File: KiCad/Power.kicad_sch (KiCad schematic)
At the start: 0 parts

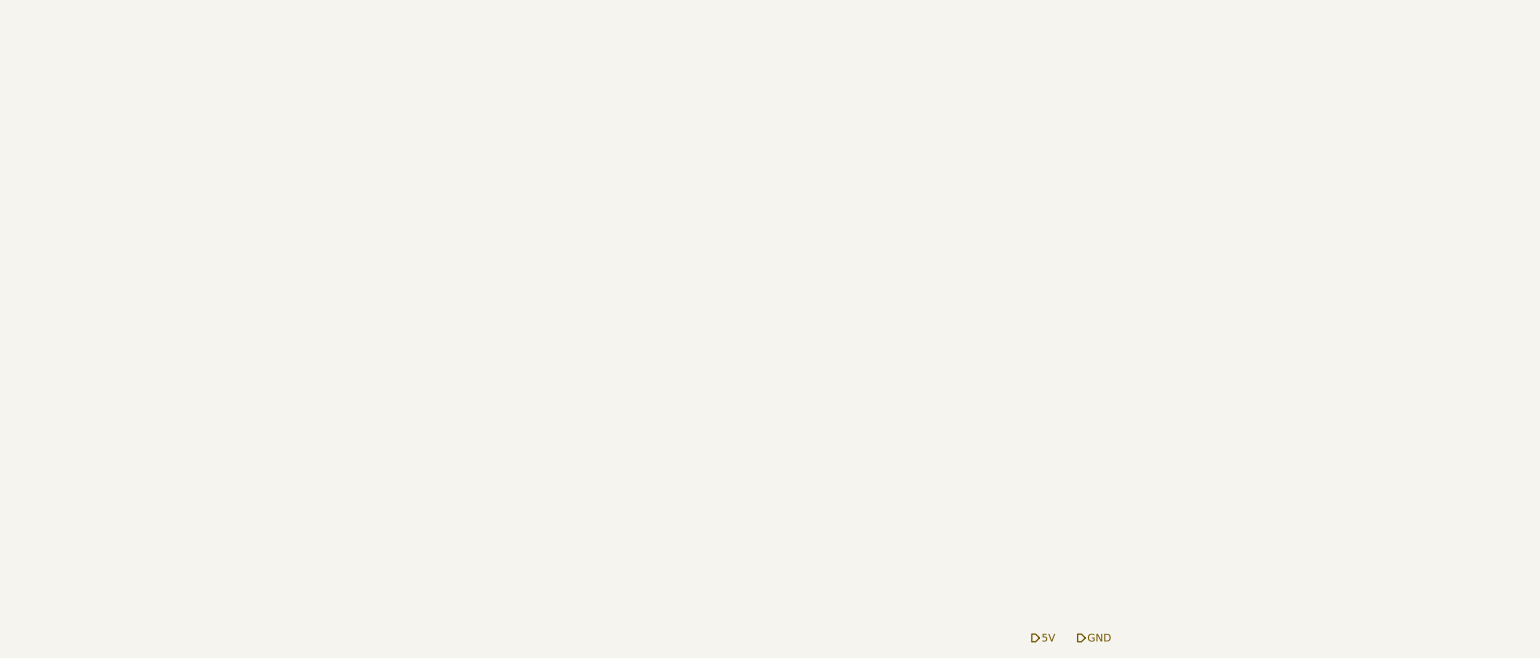
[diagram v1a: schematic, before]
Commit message: kicad power added
added the power section to kicad
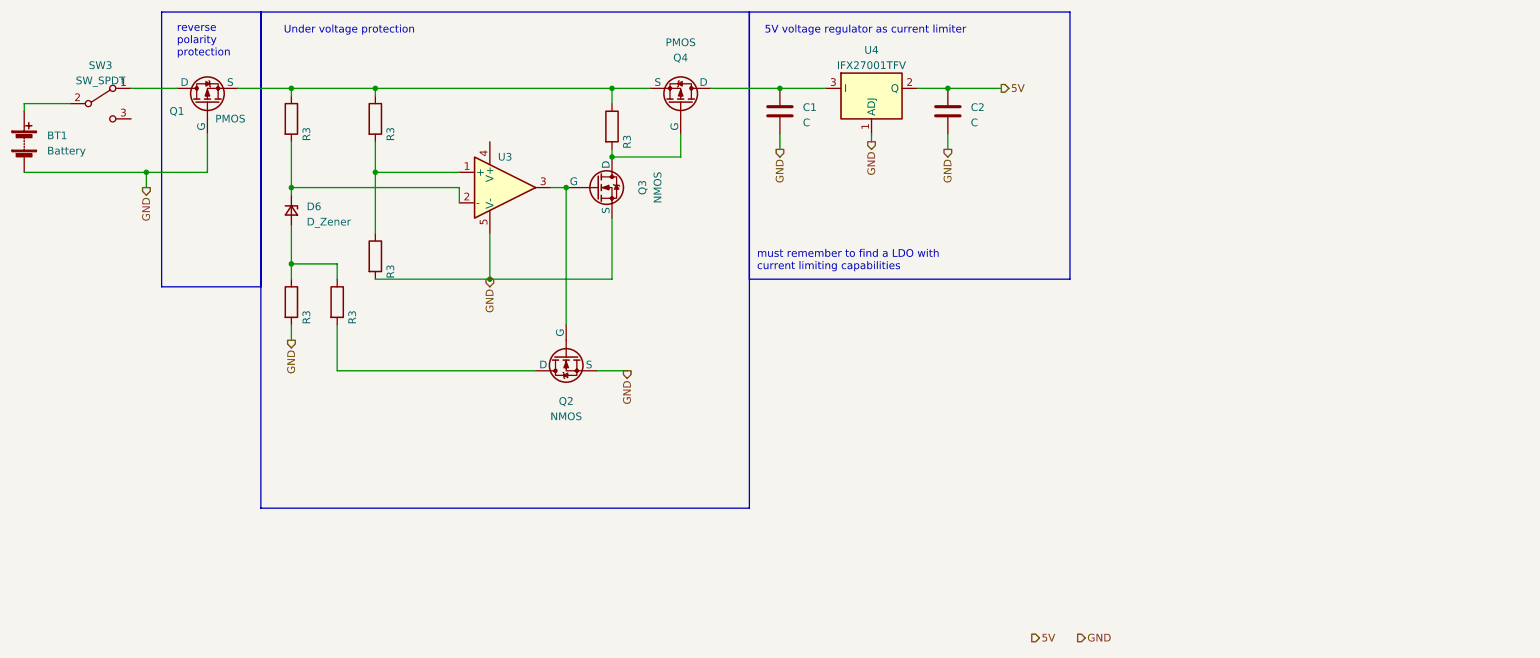
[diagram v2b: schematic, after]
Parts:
- added BT1: Battery, symbol Device:Battery
- added C1, C2: C, symbol Device:C
- added D6: D_Zener, symbol Device:D_Zener_Small
- added Q1, Q4: PMOS, symbol Simulation_SPICE:PMOS
- added Q2, Q3: NMOS, symbol Simulation_SPICE:NMOS
- added R3 (x6): ~, symbol Device:R
- added SW3: SW_SPDT, symbol Switch:SW_SPDT
- added U3: ${SIM.PARAMS}, symbol Simulation_SPICE:OPAMP
- added U4: IFX27001TFV, Package_TO_SOT_SMD:TO-252-3_TabPin2, symbol Regulator_Linear:IFX27001TFV
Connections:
- net 5V: now also C2.1, U4.2 (Q)
- net GND: now also BT1.2 (-), C1.2, C2.2, Q1.2 (G), Q2.3 (S), Q3.3 (S), R3.2, R3.2, U3.5 (V-), U4.1 (ADJ)
- new net: Q1.1 (D), SW3.1 (A)
- new net: BT1.1 (+), SW3.2 (B)
- new net: D6.2 (A), R3.1, R3.1
- new net: R3.1, R3.2, U3.1 (+)
- new net: Q1.3 (S), Q4.3 (S), R3.1, R3.1, R3.1
- new net: C1.1, Q4.1 (D), U4.3 (I)
- new net: Q3.1 (D), Q4.2 (G), R3.2
- new net: D6.1 (K), R3.2, U3.2 (-)
- new net: Q2.2 (G), Q3.2 (G), U3.3
- new net: Q2.1 (D), R3.2
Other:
- note added: "5V voltage regulator as current limiter"
- note added: "Under voltage protection"
- note added: "must remember to find a LDO with current limiting capabilities"
- note added: "reverse polarity protection"

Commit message: ki cad changes
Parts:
- removed D6: D_Zener, symbol Device:D_Zener_Small
- removed Q2, Q3: NMOS, symbol Simulation_SPICE:NMOS
- removed Q4: PMOS, symbol Simulation_SPICE:PMOS
- removed R3 (x6): ~, symbol Device:R
- removed U3: ${SIM.PARAMS}, symbol Simulation_SPICE:OPAMP
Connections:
- net 7.5V: now reaches Q1.3 (S)
- net 7.5V: now also C1.1, U4.3 (I)
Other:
- note removed: "Under voltage protection"
- moved on the sheet: BT1, C1, C2, Q1, SW3, U4

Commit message: kicad
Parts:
- added SW2: SW_SPDT, symbol Switch:SW_SPDT
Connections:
- net 7.5V renamed 7.5V arduino
- net 7.5V arduino: now also SW2.2 (B)
- new net 7.5V switch: SW2.1 (A)
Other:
- note added: "power H-brige"
- note removed: "must remember to find a LDO with current limiting capabilities"
- moved on the sheet: BT1, C1, C2, Q1, SW3, U4
